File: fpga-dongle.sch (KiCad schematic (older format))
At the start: 66 parts, among them P1 USB_PWR, P2 PGM, P3 right, P4 left, P5 CONN_01X40, P6 CONN_01X40, SW1 T1107A(6x3,8x2,5MM), U1 W25Q16BVSSIG(SOIC-8_208mil), U2 sc189(Z) 3.3v, U3 sc189(C) 1.2v, U4 iCE40-HX4K-TQ144, U5 AS4C16M16S

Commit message: Added SPI programmer with LPC11U35 as MSC
Signed-off-by: Martin Ribelotta <martinribelotta@gmail.com>
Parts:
- removed R7: 22R, Resistors_SMD:R_0805, symbol R
- added C33, C34, C36: 100nF, Capacitors_SMD:C_0805, symbol C
- added C35, C37: 10nF, Capacitors_SMD:C_0805, symbol C
- added C38, C39: 18pF, Capacitors_SMD:C_0805, symbol C
- added D3: LED, LEDs:LED_0603, symbol LED
- added F2: 1A, OLIMEX_Devices-FP:FUSE-1206, symbol F_Small
- added P7: DBG_SWD, Pin_Headers:Pin_Header_Straight_2x03, symbol CONN_01X06
- added P8: USB_PWR, OLIMEX_Connectors-FP:USB_Mini-B-NOSILK, symbol USB_OTG
- added Q1: BC857, TO_SOT_Packages_SMD:SOT-23, symbol BC857
- added R13, R14, R23: 24k, Resistors_SMD:R_0805, symbol R
- added R15, R16, R27, R30: 22R, Resistors_SMD:R_0805, symbol R
- added R17: 10k, Resistors_SMD:R_0805, symbol R
- added R19, R24, R26: 2k, Resistors_SMD:R_0805, symbol R
- added R20, R21: 33, Resistors_SMD:R_0805, symbol R
- added R22: 1.5k, Resistors_SMD:R_0805, symbol R
- added R25: UL, Resistors_SMD:R_0805, symbol R
- added R31, R32, R33, R34, R35, R36, R37, R38, R39: 100R, Resistors_SMD:R_0805, symbol R
- added U6: LPC11U35FBD48, Housings_QFP:LQFP-48_7x7mm_Pitch0.5mm, symbol LPC11U35FBD48
- added X1: 12MHz, Crystals_Oscillators_SMD:crystal_FA238-TSX3225, symbol Crystal_GND
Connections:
- net +3V3: now also C34.1, C35.1, C36.1, C37.1, P7.1 (P1), Q1.2 (E), R13.1, R17.1, R19.2, R23.1, R26.1, U6.44 (Vdd), U6.8 (Vdd)
- net +5V: now also F2.2
- net GND: now also C33.2, C34.2, C35.2, C36.2, C37.2, C38.2, C39.2, P7.6 (P6), P8.5 (GND), R14.2, R25.2, U6.41 (Vss), U6.5 (Vss), X1.3 (case)
- net GPIO0: now also R39.2
- net I2C_SCL: now also R32.2
- net I2C_SDA: now also R31.2
- net RxD: now also R37.2
- net SPI_CLK: now also R36.2
- net SPI_CS: now also R33.2
- net SPI_MISO: now also R35.2
- net SPI_MOSI: now also R34.2
- net TxD: now also R38.2
- net iCE40-CDONE: now also U6.40 (PIO0_16/AD5/CT32B1_M3)
- net iCE40-CRESET: now also U6.42 (PIO0_23/AD7)
- net iCE40-SCK: now also R16.2
- net iCE40-SDI: now also R30.2
- net iCE40-SDO: now also R27.2
- net iCE40-SS_B: now also R5.1, U1.1 (#CS), R15.2
- new net: C39.1, U6.7 (XTALOUT), X1.1
- new net: C38.1, U6.6 (XTALIN), X1.2
- new net: R19.1, U6.14 (PIO0_3/USB_Vbus)
- new net: Q1.3 (C), R22.2
- new net: Q1.1 (B), R23.2, R24.1, R25.1
- new net: D3.2 (A), R26.2
- new net: F2.1, P8.1 (VCC)
- new net DBG_SWCLK: P7.3 (P3), R14.1, U6.29 (PIO0_10/SWCLK/SCK0)
- new net DBG_SWDIO: P7.2 (P2), R13.2, U6.39 (PIO0_15/SWDIO/AD4)
- new net DBG_~ISP~: P7.5 (P5), U6.4 (PIO0_1/C32B0_M2)
- new net DBG_~RST~: C33.1, P7.4 (P4), R17.2, U6.3 (PIO0_0/~RESET)
- new net D_USB_N: R21.2, U6.19 (USB_DM)
- new net D_USB_P: R20.2, U6.20 (USB_DP)
- new net FPGM_MISO: R27.1, U6.30 (PIO0_22/MISO1/ADC6)
- new net FPGM_MOSI: R30.1, U6.38 (MOSI1/PIO1_22)
- new net FPGM_SCK: R16.1, U6.43 (SCK1/PIO1_15)
- new net FPGM_SS: R15.1, U6.18 (CT16B1_M1/SSEL1/PIO1_23)
- new net P_GPIO: R39.1, U6.25 (PIO1_31)
- new net P_RxD: R37.1, U6.46 (PIO0_18/RXD)
- new net P_SCL: R32.1, U6.16 (PIO0_5/SDA)
- new net P_SDA: R31.1, U6.15 (PIO0_4/SCL)
- new net P_SPI_CLK: R36.1, U6.31 (SCK0/CT32B0_C1/PIO1_29)
- new net P_SPI_MISO: R35.1, U6.27 (PIO0_8/MISO0/CT16B0_M0)
- new net P_SPI_MOSI: R34.1, U6.28 (PIO0_9/MOSI0/CT16B0_M1)
- new net P_SPI_SS: R33.1, U6.10 (PIO0_2/SSEL0/CT16B0_C0)
- new net P_TxD: R38.1, U6.47 (PIO0_19/TXD)
- new net USB_N: P8.2 (D-), R21.1
- new net USB_P: P8.3 (D+), R20.1, R22.1
- new net ~USB_CONNECT~: D3.1 (K), R24.2, U6.22 (PIO0_6/~USB_Connect~/SCK0)
- no-connect marks 21 -> 41
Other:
- note added: "Program and debug"
- moved on the sheet: C1, C10, C11, C12, C13, C14, C15, C16, C17, C18, C19, C2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

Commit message: Reroute SDRAM, connect to EDU-CIAA conenctor, fix schematic net tames
Signed-off-by: Martin Ribelotta <martinribelotta@gmail.com>
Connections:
- net 232_RX is gone; now on net RxD: P4.23 (P23)
- net 232_TX is gone; now on net TxD: P4.25 (P25)
- net SPI_SCK is gone; now on net SPI_CLK: P3.20 (P20)
- net BUT1: now also P5.23 (P23)
- net EXTCLK: now also P5.24 (P24)
- net FPGA_IO_BANK1_14: now also P5.25 (P25); no longer P5.23 (P23)
- net FPGA_IO_BANK1_15: now also P5.26 (P26); no longer P5.24 (P24)
- net FPGA_IO_BANK1_16: now also P5.27 (P27); no longer P5.25 (P25)
- net FPGA_IO_BANK1_17: now also P5.28 (P28); no longer P5.26 (P26)
- net FPGA_IO_BANK1_18: now also P5.29 (P29); no longer P5.27 (P27)
- net FPGA_IO_BANK1_19: now also P5.30 (P30); no longer P5.28 (P28)
- net FPGA_IO_BANK1_20: now also P5.31 (P31); no longer P5.29 (P29)
- net FPGA_IO_BANK1_21: now also P5.32 (P32); no longer P5.30 (P30)
- net FPGA_IO_BANK1_22: now also P5.33 (P33); no longer P5.31 (P31)
- net FPGA_IO_BANK1_23: now also P5.34 (P34); no longer P5.32 (P32)
- net RAM_A1: now also U4.76 (IOR_112); no longer U4.75 (IOR_111)
- net RAM_A10: now also U4.56 (IOB_94); no longer U4.55 (IOB_91)
- net RAM_A11: now also U4.78 (IOR_114); no longer U4.76 (IOR_112)
- net RAM_A12: now also U4.55 (IOB_91); no longer U4.52 (IOB_82_GBIN4)
- net RAM_A13: now also U4.52 (IOB_82_GBIN4); no longer U4.49 (IOB_81_GBIN5)
- net RAM_A14: now also U4.80 (IOR_116); no longer U4.79 (IOR_115)
- net RAM_A15: now also U4.79 (IOR_115); no longer U4.78 (IOR_114)
- net RAM_A2: now also U4.75 (IOR_111); no longer U4.74 (IOR_110)
- net RAM_A3: now also U4.74 (IOR_110); no longer U4.73 (IOR_109)
- net RAM_A4: now also U4.73 (IOR_109); no longer U4.64 (IOB_104_CBSEL1)
- net RAM_A5: now also U4.64 (IOB_104_CBSEL1); no longer U4.63 (IOB_103_CBSEL0)
- net RAM_A6: now also U4.63 (IOB_103_CBSEL0); no longer U4.62 (IOB_102)
- net RAM_A7: now also U4.62 (IOB_102); no longer U4.61 (IOB_96)
- net RAM_A8: now also U4.61 (IOB_96); no longer U4.60 (IOB_95)
- net RAM_A9: now also U4.60 (IOB_95); no longer U4.56 (IOB_94)
- net RAM_CAS: now also U4.83 (IOR_119); no longer U4.82 (IOR_118)
- net RAM_CKE: now also U4.49 (IOB_81_GBIN5); no longer U4.48 (IOB_80)
- net RAM_CLK: now also U4.48 (IOB_80); no longer U4.47 (IOB_79)
- net RAM_CS: now also U4.81 (IOR_117); no longer U4.80 (IOR_116)
- net RAM_D0: now also U4.96 (IOR_146); no longer U4.95 (IOR_144)
- net RAM_D1: now also U4.95 (IOR_144); no longer U4.94 (IOR_141_GBIN2)
- net RAM_D10: now also U4.43 (IOB_71); no longer U4.42 (IOB_64)
- net RAM_D11: now also U4.42 (IOB_64); no longer U4.41 (IOB_63)
- net RAM_D12: now also U4.41 (IOB_63); no longer U4.39 (IOB_61)
- net RAM_D13: now also U4.39 (IOB_61); no longer U4.38 (IOB_57)
- net RAM_D14: now also U4.38 (IOB_57); no longer U4.37 (IOB_56)
- net RAM_D15: now also U4.37 (IOB_56); no longer U4.96 (IOR_146)
- net RAM_D2: now also U4.94 (IOR_141_GBIN2); no longer U4.93 (IOR_140_GBIN3)
- net RAM_D3: now also U4.93 (IOR_140_GBIN3); no longer U4.91 (IOR_139)
- net RAM_D4: now also U4.91 (IOR_139); no longer U4.90 (IOR_138)
- net RAM_D5: now also U4.90 (IOR_138); no longer U4.88 (IOR_137)
- net RAM_D6: now also U4.88 (IOR_137); no longer U4.87 (IOR_136)
- net RAM_D7: now also U4.87 (IOR_136); no longer U4.85 (IOR_128)
- net RAM_D8: now also U4.45 (IOB_73); no longer U4.44 (IOB_72)
- net RAM_D9: now also U4.44 (IOB_72); no longer U4.43 (IOB_71)
- net RAM_DQMH: now also U4.47 (IOB_79); no longer U4.45 (IOB_73)
- net RAM_DQML: now also U4.85 (IOR_128); no longer U4.84 (IOR_120)
- net RAM_RAS: now also U4.82 (IOR_118); no longer U4.81 (IOR_117)
- net RAM_RDnWR: now also U4.84 (IOR_120); no longer U4.83 (IOR_119)
- no-connect marks 41 -> 39
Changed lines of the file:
@@
 	-1   0    0    -1
 $EndComp
+Text Label 10550 3325 0    60   ~ 0
+RAM_D1
 Text Label 10550 3225 0    60   ~ 0
-RAM_D1
+RAM_D2
 Text Label 10550 3125 0    60   ~ 0
-RAM_D2
+RAM_D3
 Text Label 10550 3025 0    60   ~ 0
-RAM_D3
+RAM_D4
 Text Label 10550 2925 0    60   ~ 0
-RAM_D4
+RAM_D5
 Text Label 10550 2825 0    60   ~ 0
-RAM_D5
+RAM_D6
 Text Label 10550 2725 0    60   ~ 0
-RAM_D6
+RAM_D7
+Text Label 10550 1825 0    60   ~ 0
+RAM_A1
+Text Label 10550 1725 0    60   ~ 0
+RAM_A2
+Text Label 10550 1625 0    60   ~ 0
+RAM_A3
+Text Label 10550 1525 0    60   ~ 0
+RAM_A4
+Text Label 10550 1925 0    60   ~ 0
+RAM_A11
+Text Label 10550 2125 0    60   ~ 0
+RAM_A14
+Text Label 10550 2025 0    60   ~ 0
+RAM_A15
+Text Label 10550 2225 0    60   ~ 0
+RAM_CS
+Text Label 10550 2325 0    60   ~ 0
+RAM_RAS
+Text Label 10550 2425 0    60   ~ 0
+RAM_CAS
 Text Label 10550 2625 0    60   ~ 0
-RAM_D7
-Text Label 10550 1725 0    60   ~ 0
-RAM_A1
-Text Label 10550 1625 0    60   ~ 0
-RAM_A2
-Text Label 10550 1525 0    60   ~ 0
-RAM_A3
+RAM_DQML
+Text Label 10550 2525 0    60   ~ 0
+RAM_RDnWR
+Text Label 10550 3425 0    60   ~ 0
+RAM_D0
+Text Label 8150 2425 2    60   ~ 0
+RAM_D8
+Text Label 8150 2325 2    60   ~ 0
+RAM_D9
+Text Label 8150 2225 2    60   ~ 0
+RAM_D10
+Text Label 8150 2125 2    60   ~ 0
+RAM_D11
+Text Label 8150 2025 2    60   ~ 0
+RAM_D12
+Text Label 8150 1925 2    60   ~ 0
+RAM_D13
+Text Label 8150 1825 2    60   ~ 0
+RAM_D14
 Text Label 8150 3525 2    60   ~ 0
-RAM_A4
-Text Label 10550 1825 0    60   ~ 0
-RAM_A11
-Text Label 10550 2025 0    60   ~ 0
-RAM_A14
-Text Label 10550 1925 0    60   ~ 0
-RAM_A15
-Text Label 10550 2125 0    60   ~ 0
-RAM_CS
-Text Label 10550 2225 0    60   ~ 0
-RAM_RAS
-Text Label 10550 2325 0    60   ~ 0
-RAM_CAS
-Text Label 10550 2525 0    60   ~ 0
-RAM_DQML
-Text Label 10550 2425 0    60   ~ 0
-RAM_RDnWR
-Text Label 10550 3325 0    60   ~ 0
-RAM_D0
-Text Label 8150 2325 2    60   ~ 0
-RAM_D8
-Text Label 8150 2225 2    60   ~ 0
-RAM_D9
-Text Label 8150 2125 2    60   ~ 0
-RAM_D10
-Text Label 8150 2025 2    60   ~ 0
-RAM_D11
-Text Label 8150 1925 2    60   ~ 0
-RAM_D12
-Text Label 8150 1825 2    60   ~ 0
-RAM_D13
+RAM_A5
+Text Label 8150 3425 2    60   ~ 0
+RAM_A6
+Text Label 8150 3325 2    60   ~ 0
+RAM_A7
+Text Label 8150 3225 2    60   ~ 0
+RAM_A8
+Text Label 8150 3125 2    60   ~ 0
+RAM_A9
+Text Label 8150 3025 2    60   ~ 0
+RAM_A10
+Text Label 8150 2925 2    60   ~ 0
+RAM_A12
+Text Label 8150 2825 2    60   ~ 0
+RAM_A13
+Text Label 8150 2725 2    60   ~ 0
+RAM_CKE
+Text Label 8150 2525 2    60   ~ 0
+RAM_DQMH
+Text Label 8150 2625 2    60   ~ 0
+RAM_CLK
 Text Label 8150 1725 2    60   ~ 0
-RAM_D14
-Text Label 8150 3425 2    60   ~ 0
-RAM_A5
-Text Label 8150 3325 2    60   ~ 0
-RAM_A6
-Text Label 8150 3225 2    60   ~ 0
-RAM_A7
-Text Label 8150 3125 2    60   ~ 0
-RAM_A8
-Text Label 8150 3025 2    60   ~ 0
-RAM_A9
-Text Label 8150 2925 2    60   ~ 0
-RAM_A10
-Text Label 8150 2825 2    60   ~ 0
-RAM_A12
-Text Label 8150 2725 2    60   ~ 0
-RAM_A13
-Text Label 8150 2625 2    60   ~ 0
-RAM_CKE
-Text Label 8150 2425 2    60   ~ 0
-RAM_DQMH
-Text Label 8150 2525 2    60   ~ 0
-RAM_CLK
-Text Label 10550 3425 0    60   ~ 0
 RAM_D15
 Text Label 10650 8925 0    60   ~ 0
@@
 SPI_MOSI
 Text Label 14300 2325 0    60   ~ 0
-SPI_SCK
+SPI_CLK
 Text Label 14300 2225 0    60   ~ 0
 SPI_MISO
@@
 CAN_TD
 Text Label 15100 2525 2    60   ~ 0
-232_RX
+RxD
 Text Label 15100 2625 2    60   ~ 0
-232_TX
+TxD
 Text Label 15100 2425 2    60   ~ 0
 I2C_SCL
@@
 Text Label 5025 7700 0    60   ~ 0
 FPGA_IO_BANK1_13
-Text Label 5025 7800 0    60   ~ 0
+Text Label 5025 8000 0    60   ~ 0
 FPGA_IO_BANK1_14
-Text Label 5025 7900 0    60   ~ 0
+Text Label 5025 8100 0    60   ~ 0
 FPGA_IO_BANK1_15
-Text Label 5025 8000 0    60   ~ 0
+Text Label 5025 8200 0    60   ~ 0
 FPGA_IO_BANK1_16
-Text Label 5025 8100 0    60   ~ 0
+Text Label 5025 8300 0    60   ~ 0
 FPGA_IO_BANK1_17
-Text Label 5025 8200 0    60   ~ 0
+Text Label 5025 8400 0    60   ~ 0
 FPGA_IO_BANK1_18
-Text Label 5025 8300 0    60   ~ 0
+Text Label 5025 8500 0    60   ~ 0
 FPGA_IO_BANK1_19
-Text Label 5025 8400 0    60   ~ 0
+Text Label 5025 8600 0    60   ~ 0
 FPGA_IO_BANK1_20
-Text Label 5025 8500 0    60   ~ 0
+Text Label 5025 8700 0    60   ~ 0
 FPGA_IO_BANK1_21
-Text Label 5025 8600 0    60   ~ 0
+Text Label 5025 8800 0    60   ~ 0
 FPGA_IO_BANK1_22
-Text Label 5025 8700 0    60   ~ 0
+Text Label 5025 8900 0    60   ~ 0
 FPGA_IO_BANK1_23
 Text Label 6350 6175 0    60   ~ 0
@@
 NoConn ~ 5025 6200
 NoConn ~ 5025 6300
-NoConn ~ 5025 8800
-NoConn ~ 5025 8900
 NoConn ~ 5025 9000
 NoConn ~ 5025 9100
@@
 	9750 13525 9850 13525
 Connection ~ 9750 13375
+Text Label 5025 7800 0    60   ~ 0
+BUT1
+Text Label 5025 7900 0    60   ~ 0
+EXTCLK
 $EndSCHEMATC

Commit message: Fix CIAA connector side error, power net route
Signed-off-by: Martin Ribelotta <martinribelotta@gmail.com>
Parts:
- added R18, R28, R29, R40, R41, R7: 100R, Resistors_SMD:R_0805, symbol R
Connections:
- net GNDA is gone; now on net GND: P4.10 (P10), P4.12 (P12), P4.14 (P14), P4.16 (P16), P4.18 (P18), P4.8 (P8)
- net GPIO0: now also U4.102 (IOR_161); no longer U4.107 (IOR_167)
- net I2C_SCL: now also U4.106 (IOR_166); no longer U4.98 (IOR_148)
- net I2C_SDA: now also U4.107 (IOR_167); no longer U4.97 (IOR_147)
- net P_RxD: now also R38.1; no longer R37.1
- net P_TxD: now also R37.1; no longer R38.1
- net RxD: now also R38.2; no longer R37.2
- net SPI_CLK: now also U4.98 (IOR_148); no longer U4.104 (IOR_164)
- net SPI_CS: now also U4.101 (IOR_160); no longer U4.99 (IOR_152)
- net SPI_MISO: now also U4.97 (IOR_147); no longer U4.102 (IOR_161)
- net SPI_MOSI: now also U4.99 (IOR_152); no longer U4.101 (IOR_160)
- net TxD: now also R37.2, U4.104 (IOR_164); no longer R38.2, U4.106 (IOR_166)
- net iCE40-CDONE: now also R40.2
- net iCE40-CRESET: now also R41.2
- net iCE40-SCK: now also R29.2
- net iCE40-SDI: now also R18.2
- net iCE40-SDO: now also R7.2
- net iCE40-SS_B: now also R28.2
- net AUX_CRESET: now reaches P3.12 (P12)
- net AUX_CRESET: now also R41.1
- net AUX_CDONE: now reaches P3.14 (P14)
- net AUX_CDONE: now also R40.1
- net AUX_SPI_SCK: now reaches P3.15 (P15)
- net AUX_SPI_SCK: now also R29.1
- net AUX_SPI_SSEL: now reaches P3.16 (P16)
- net AUX_SPI_SSEL: now also R28.1
- net AUX_SPI_MISO: now reaches P3.4 (P4)
- net AUX_SPI_MISO: now also R7.1
- net AUX_SPI_MOSI: now reaches P3.6 (P6)
- net AUX_SPI_MOSI: now also R18.1
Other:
- moved on the sheet: R31, R32, R33, R34, R35, R36, R37, R38, R39

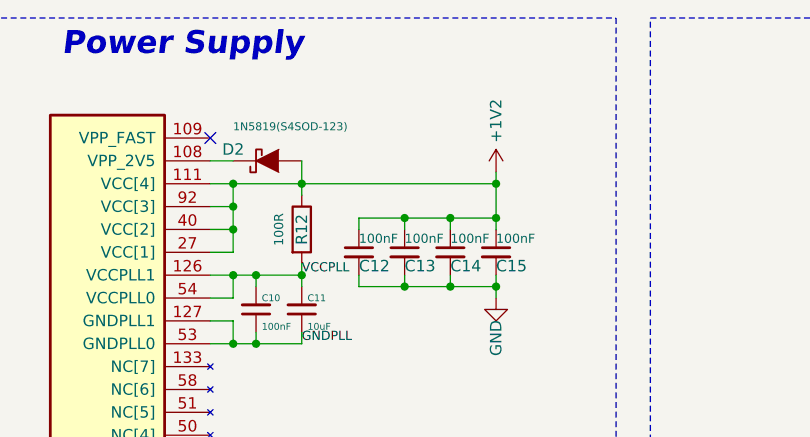
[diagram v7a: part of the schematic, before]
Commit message: Fix 2V5 net diode from 1v2 to 3v3
Signed-off-by: Martin Ribelotta <martinribelotta@gmail.com>
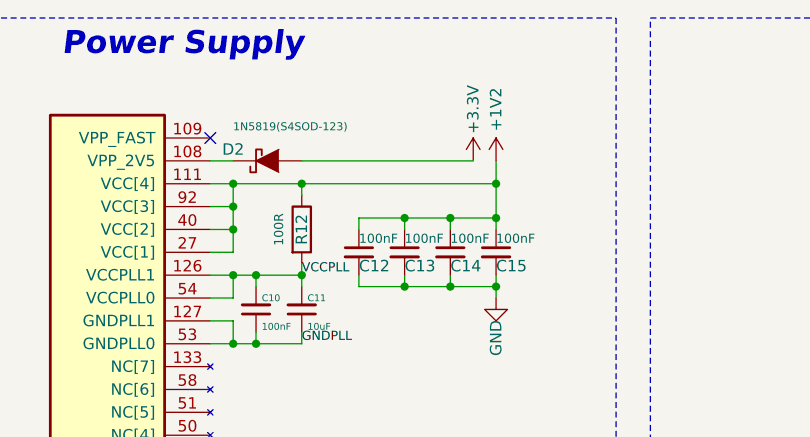
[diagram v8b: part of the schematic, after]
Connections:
- net +1V2: no longer D2.2 (A)
- net +3V3: now also D2.2 (A)
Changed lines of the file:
@@
 L +1V2 #PWR056
 U 1 1 57D4ACC4
-P 5425 1450
-F 0 "#PWR056" H 5425 1300 50  0001 C CNN
-F 1 "+1V2" V 5425 1675 50  0000 C CNN
-F 2 "" H 5425 1450 60  0000 C CNN
-F 3 "" H 5425 1450 60  0000 C CNN
-	1    5425 1450
+P 5425 1400
+F 0 "#PWR056" H 5425 1250 50  0001 C CNN
+F 1 "+1V2" V 5425 1625 50  0000 C CNN
+F 2 "" H 5425 1400 60  0000 C CNN
+F 3 "" H 5425 1400 60  0000 C CNN
+	1    5425 1400
 	1    0    0    -1
 $EndComp
@@
 Wire Wire Line
 	4275 1400 4175 1400
-Wire Wire Line
-	4575 1400 4575 1550
 Connection ~ 4575 1500
 Wire Wire Line
@@
 Connection ~ 5025 1650
 Wire Wire Line
-	5425 1450 5425 1700
+	5425 1400 5425 1700
 Connection ~ 5425 1650
 Connection ~ 5425 1500
@@
 	0    -1   1    0
 $EndComp
+$Comp
+L +3.3V #PWR?
+U 1 1 57EDAE15
+P 5325 1400
+F 0 "#PWR?" H 5325 1250 50  0001 C CNN
+F 1 "+3.3V" V 5325 1625 50  0000 C CNN
+F 2 "" H 5325 1400 60  0000 C CNN
+F 3 "" H 5325 1400 60  0000 C CNN
+	1    5325 1400
+	-1   0    0    -1
+$EndComp
+Wire Wire Line
+	4575 1500 4575 1550
+Wire Wire Line
+	4575 1400 5325 1400
 $EndSCHEMATC
